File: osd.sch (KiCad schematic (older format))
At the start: 24 parts, among them U6 LMH1980, U7 TS5A3160, U8 TS5A3160, U9 LT6206

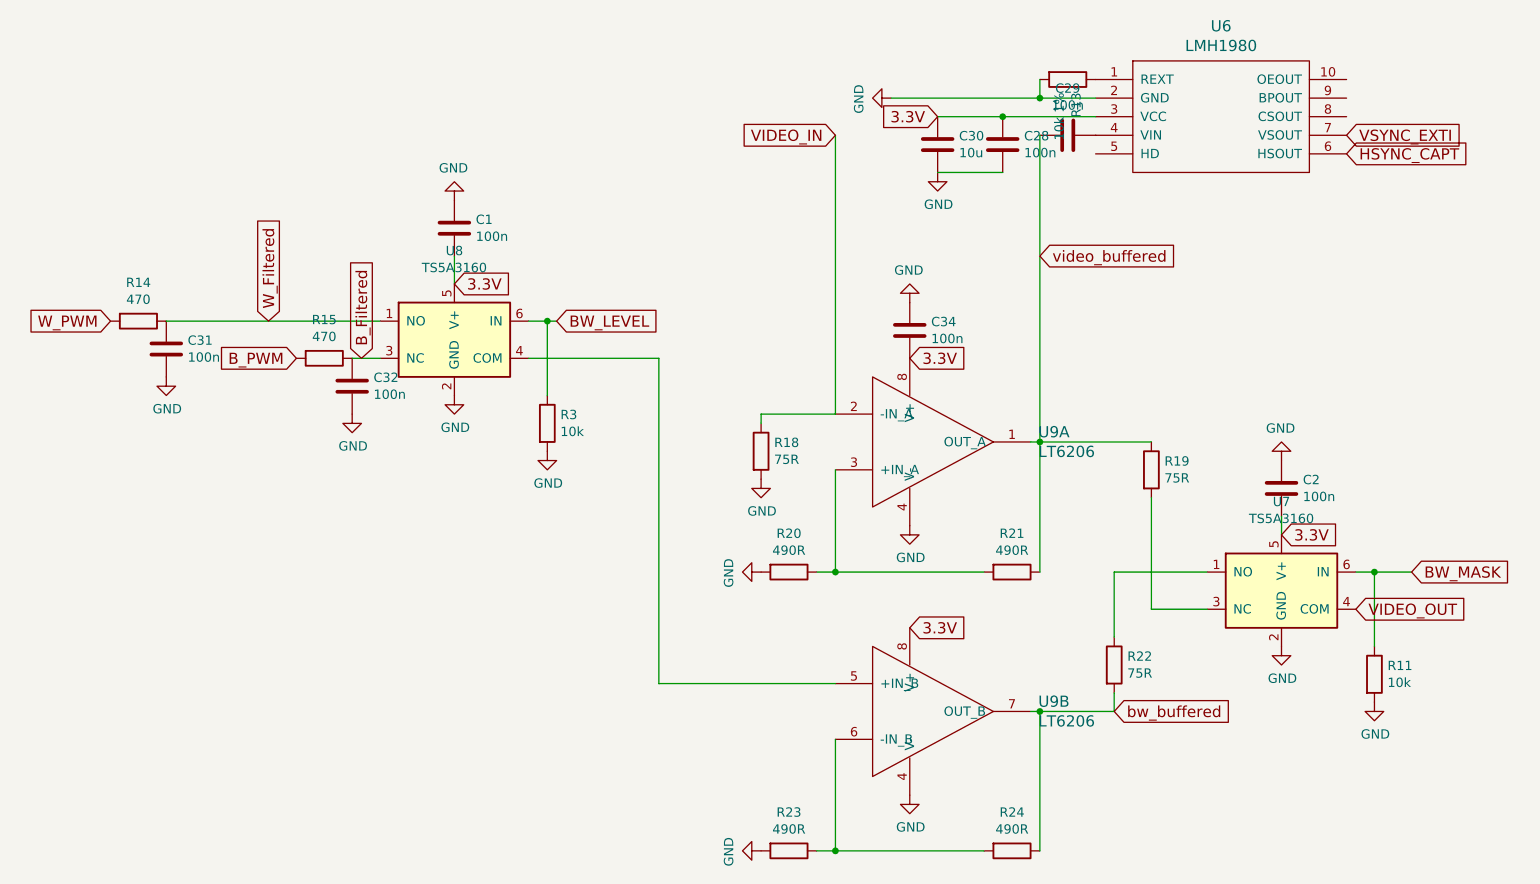
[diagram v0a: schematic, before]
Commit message: fixed video opamp and output switch circuit, removed line termination resistors
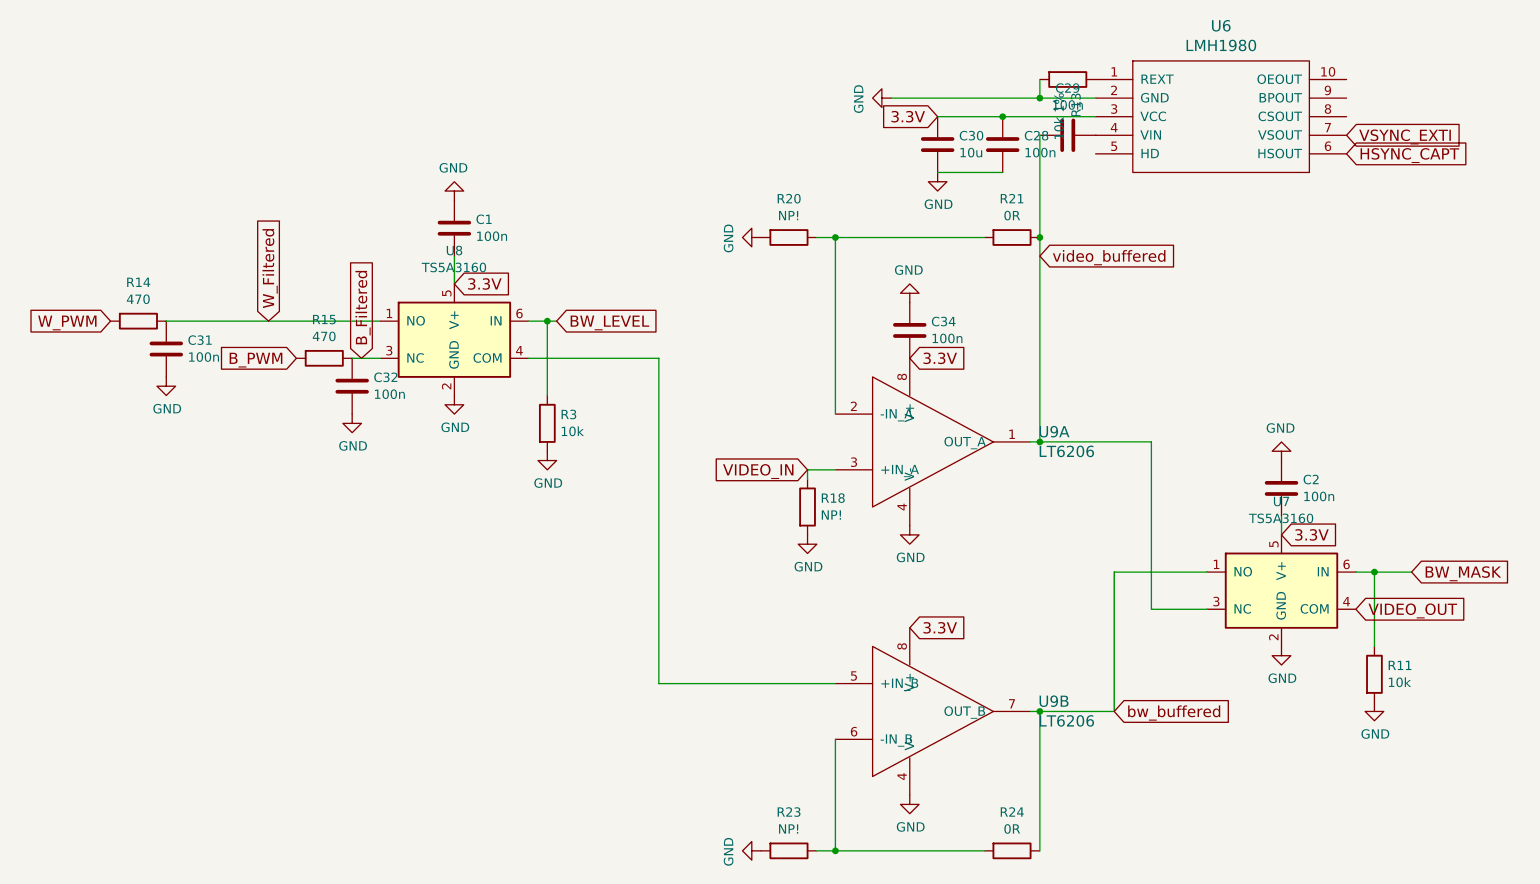
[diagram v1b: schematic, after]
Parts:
- removed R19, R22: 75R, Resistors_SMD:R_0402, symbol R
- R18: value 75R -> NP!
- R20, R23: value 490R -> NP!
- R21, R24: value 490R -> 0R
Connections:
- net VIDEO_IN: now also U9.3 (+IN_A); no longer U9.2 (-IN_A)
- net bw_buffered: now also U7.1 (NO)
- net video_buffered: now also U7.3 (NC)
- net at R20.1, R21.2: now also U9.2 (-IN_A); no longer U9.3 (+IN_A)
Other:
- moved on the sheet: R18, R20, R21
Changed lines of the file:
@@
 Wire Wire Line
 	3450 3750 4150 3750
-Text GLabel 5100 2550 0    60   Input ~ 0
+Text GLabel 4950 4350 0    60   Input ~ 0
 VIDEO_IN
 $Comp
@@
 Text GLabel 5500 5200 2    60   Input ~ 0
 3.3V
-$Comp
-L R R22
-U 1 1 574C734F
-P 6600 5400
-F 0 "R22" H 6670 5446 50  0000 L CNN
-F 1 "75R" H 6670 5355 50  0000 L CNN
-F 2 "Resistors_SMD:R_0402" V 6530 5400 50  0001 C CNN
-F 3 "" H 6600 5400 50  0000 C CNN
-	1    6600 5400
-	1    0    0    -1
-$EndComp
-$Comp
-L R R19
-U 1 1 574C73A7
-P 6800 4350
-F 0 "R19" H 6870 4396 50  0000 L CNN
-F 1 "75R" H 6870 4305 50  0000 L CNN
-F 2 "Resistors_SMD:R_0402" V 6730 4350 50  0001 C CNN
-F 3 "" H 6800 4350 50  0000 C CNN
-	1    6800 4350
-	1    0    0    -1
-$EndComp
-Wire Wire Line
-	6600 5650 6600 5550
-Wire Wire Line
-	5100 4050 5100 2550
+Wire Wire Line
+	6600 4900 6600 5650
 Wire Wire Line
 	5100 5500 4150 5500
@@
 L R R21
 U 1 1 574C7C9D
-P 6050 4900
-F 0 "R21" V 5843 4900 50  0000 C CNN
-F 1 "490R" V 5934 4900 50  0000 C CNN
-F 2 "Resistors_SMD:R_0402" V 5980 4900 50  0001 C CNN
-F 3 "" H 6050 4900 50  0000 C CNN
-	1    6050 4900
+P 6050 3100
+F 0 "R21" V 5843 3100 50  0000 C CNN
+F 1 "0R" V 5934 3100 50  0000 C CNN
+F 2 "Resistors_SMD:R_0402" V 5980 3100 50  0001 C CNN
+F 3 "" H 6050 3100 50  0000 C CNN
+	1    6050 3100
 	0    1    1    0
 $EndComp
@@
 P 6050 6400
 F 0 "R24" V 5843 6400 50  0000 C CNN
-F 1 "490R" V 5934 6400 50  0000 C CNN
+F 1 "0R" V 5934 6400 50  0000 C CNN
 F 2 "Resistors_SMD:R_0402" V 5980 6400 50  0001 C CNN
 F 3 "" H 6050 6400 50  0000 C CNN
@@
 P 4850 6400
 F 0 "R23" V 4643 6400 50  0000 C CNN
-F 1 "490R" V 4734 6400 50  0000 C CNN
+F 1 "NP!" V 4734 6400 50  0000 C CNN
 F 2 "Resistors_SMD:R_0402" V 4780 6400 50  0001 C CNN
 F 3 "" H 4850 6400 50  0000 C CNN
@@
 L R R20
 U 1 1 574C7F13
-P 4850 4900
-F 0 "R20" V 4643 4900 50  0000 C CNN
-F 1 "490R" V 4734 4900 50  0000 C CNN
-F 2 "Resistors_SMD:R_0402" V 4780 4900 50  0001 C CNN
-F 3 "" H 4850 4900 50  0000 C CNN
-	1    4850 4900
+P 4850 3100
+F 0 "R20" V 4643 3100 50  0000 C CNN
+F 1 "NP!" V 4734 3100 50  0000 C CNN
+F 2 "Resistors_SMD:R_0402" V 4780 3100 50  0001 C CNN
+F 3 "" H 4850 3100 50  0000 C CNN
+	1    4850 3100
 	0    1    1    0
 $EndComp
@@
 	6200 6400 6200 5650
 Connection ~ 6200 5650
-Wire Wire Line
-	6200 2550 6200 4900
 Connection ~ 6200 4200
 Wire Wire Line
-	5900 4900 5000 4900
-Wire Wire Line
-	5100 4350 5100 4900
-Connection ~ 5100 4900
+	5900 3100 5000 3100
+Connection ~ 5100 3100
 Wire Wire Line
 	5000 6400 5900 6400
@@
 L GND #PWR035
 U 1 1 574C8177
-P 4700 4900
-F 0 "#PWR035" H 4700 4650 50  0001 C CNN
-F 1 "GND" H 4705 4727 50  0000 C CNN
-F 2 "" H 4700 4900 50  0000 C CNN
-F 3 "" H 4700 4900 50  0000 C CNN
-	1    4700 4900
+P 4700 3100
+F 0 "#PWR035" H 4700 2850 50  0001 C CNN
+F 1 "GND" H 4705 2927 50  0000 C CNN
+F 2 "" H 4700 3100 50  0000 C CNN
+F 3 "" H 4700 3100 50  0000 C CNN
+	1    4700 3100
 	0    1    1    0
 $EndComp
@@
 L R R18
 U 1 1 574C8713
-P 4700 4250
-F 0 "R18" H 4770 4296 50  0000 L CNN
-F 1 "75R" H 4770 4205 50  0000 L CNN
-F 2 "Resistors_SMD:R_0402" V 4630 4250 50  0001 C CNN
-F 3 "" H 4700 4250 50  0000 C CNN
-	1    4700 4250
+P 4950 4550
+F 0 "R18" H 5020 4596 50  0000 L CNN
+F 1 "NP!" H 5020 4505 50  0000 L CNN
+F 2 "Resistors_SMD:R_0402" V 4880 4550 50  0001 C CNN
+F 3 "" H 4950 4550 50  0000 C CNN
+	1    4950 4550
 	1    0    0    -1
 $EndComp
@@
 L GND #PWR038
 U 1 1 574C8818
-P 4700 4400
-F 0 "#PWR038" H 4700 4150 50  0001 C CNN
-F 1 "GND" H 4705 4227 50  0000 C CNN
-F 2 "" H 4700 4400 50  0000 C CNN
-F 3 "" H 4700 4400 50  0000 C CNN
-	1    4700 4400
-	1    0    0    -1
-$EndComp
-Wire Wire Line
-	4700 4100 4700 4050
-Wire Wire Line
-	4700 4050 5100 4050
+P 4950 4700
+F 0 "#PWR038" H 4950 4450 50  0001 C CNN
+F 1 "GND" H 4955 4527 50  0000 C CNN
+F 2 "" H 4950 4700 50  0000 C CNN
+F 3 "" H 4950 4700 50  0000 C CNN
+	1    4950 4700
+	1    0    0    -1
+$EndComp
+Wire Wire Line
+	4950 4400 4950 4350
 $Comp
 L LMH1980 U6
@@
 B_Filtered
 Wire Wire Line
-	6150 5650 6600 5650
+	6600 5650 6150 5650
 Wire Wire Line
 	6150 4200 6800 4200
 Wire Wire Line
-	6800 4500 6800 5100
+	6800 4200 6800 5100
 Wire Wire Line
 	6800 5100 7100 5100
@@
 	7100 4900 6600 4900
 Wire Wire Line
-	6600 4900 6600 5250
+	4950 4350 5100 4350
+Wire Wire Line
+	5100 3100 5100 4050
+Wire Wire Line
+	6200 4200 6200 2550
+Connection ~ 6200 3100
 $EndSCHEMATC
